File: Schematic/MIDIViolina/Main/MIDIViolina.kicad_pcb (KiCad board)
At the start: 2 copper layers, 149.9 x 101.6 mm, 152 parts, among them J1 Motor, J10 Solenoid, J11 Solenoid, J12 Solenoid, J13 Solenoid, J14 Solenoid, J15 Solenoid, J16 Solenoid, J17 Solenoid, J18 Solenoid, J19 Solenoid, J2 Motor, J20 Solenoid, J21 Solenoid, J22 Solenoid, J23 Solenoid, J24 Solenoid, J25 Solenoid, J26 Solenoid, J27 Solenoid, J28 Solenoid, J29 Solenoid, J3 Motor, J30 Solenoid, J31 Solenoid, J32 Solenoid, J33 Solenoid, J34 Solenoid, J35 Solenoid, J36 Solenoid, J37 Solenoid, J38 Solenoid, J39 Solenoid, J4 Motor, J40 Solenoid, J41 Solenoid, J5 Power in, J6 MSB 2, J7 Microstep Bridge, J8 MIDI I/O, J9 STEPPER OUT, Q1 IRF540N, Q10 IRF540N, Q11 IRF540N, Q12 IRF540N, Q13 IRF540N, Q14 IRF540N, Q15 IRF540N, Q16 IRF540N, Q17 IRF540N, Q18 IRF540N, Q19 IRF540N, Q2 IRF540N, Q20 IRF540N, Q21 IRF540N, Q22 IRF540N, Q23 IRF540N, Q24 IRF540N, Q25 IRF540N, Q26 IRF540N, Q27 IRF540N, Q28 IRF540N, Q29 IRF540N, Q3 IRF540N, Q30 IRF540N, Q31 IRF540N, Q32 IRF540N, Q33 IRF540N, Q34 IRF540N, Q35 IRF540N, Q36 IRF540N, Q4 IRF540N, Q5 IRF540N, Q6 IRF540N, Q7 IRF540N, Q8 IRF540N, Q9 IRF540N, U1 LM7805_TO220, U2 ESP32-DEVKIT-V1, U3 74AHC595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

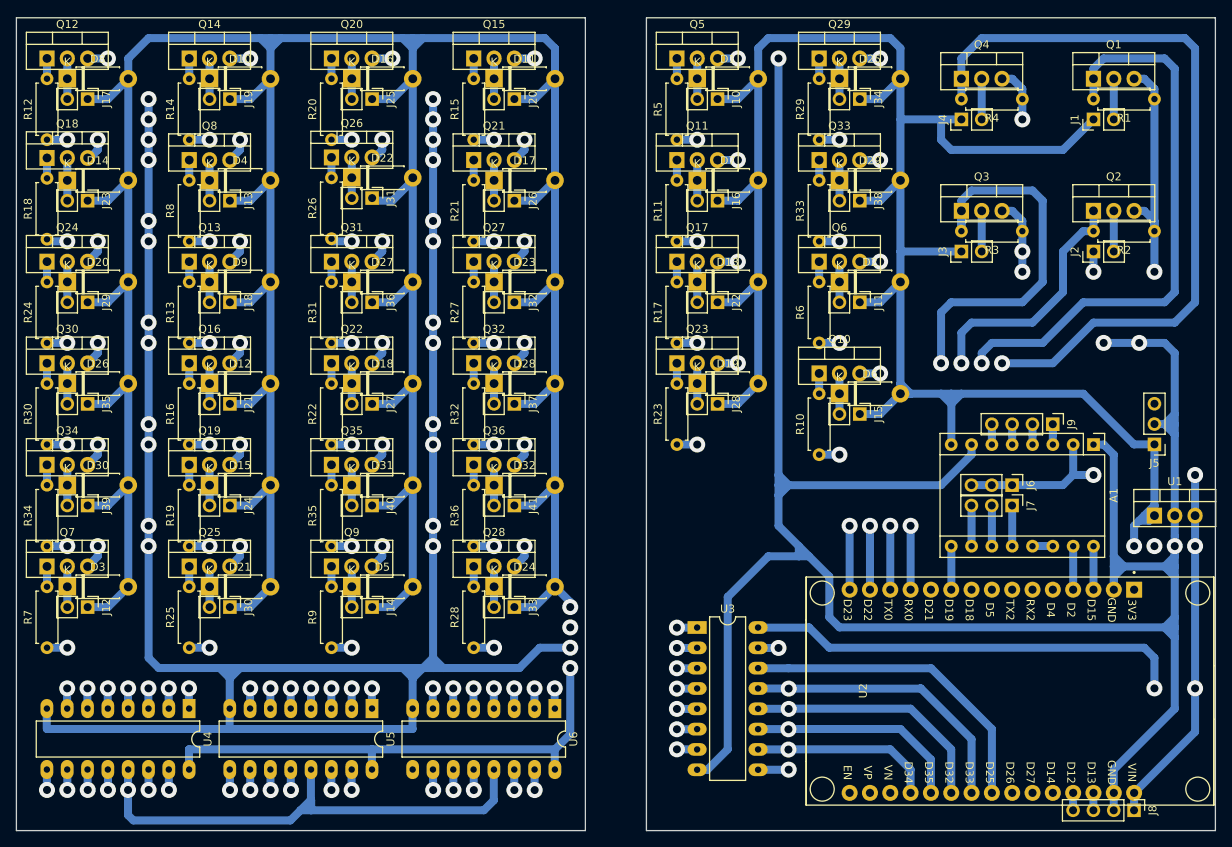
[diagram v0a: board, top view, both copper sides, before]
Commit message: CNC Toolpaths and PCB updates
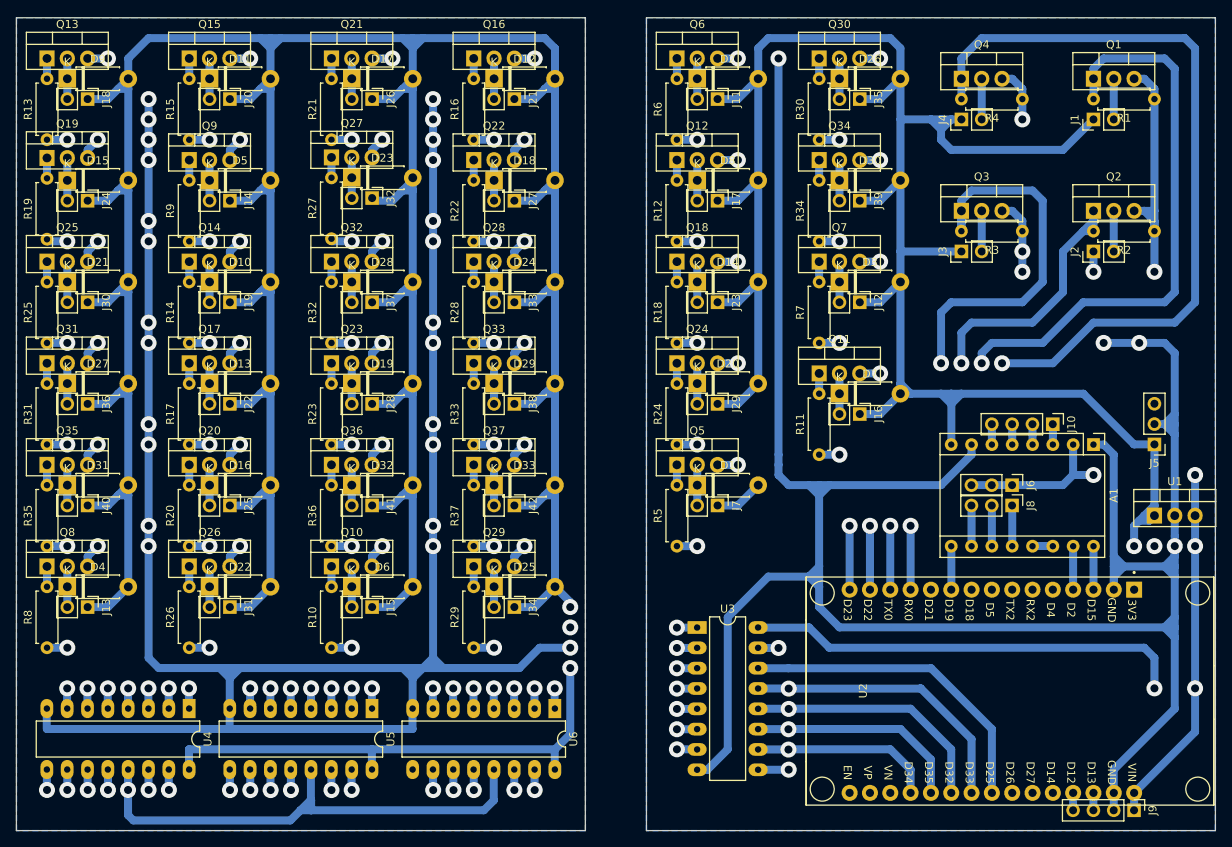
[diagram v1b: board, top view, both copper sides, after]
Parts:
- added D1: IN4001, Diode_THT:D_DO-41_SOD81_P7.62mm_Horizontal, F.Cu at (153.7, 96.5)
- added J7: Solenoid, Connector_PinHeader_2.54mm:PinHeader_1x02_P2.54mm_Vertical, F.Cu at (156.2, 99.1)
- added Q5: IRF540N, Package_TO_SOT_THT:TO-220-3_Vertical, F.Cu at (151.1, 94.0)
- added R5: 220, Resistor_THT:R_Axial_DIN0207_L6.3mm_D2.5mm_P7.62mm_Horizontal, F.Cu at (151.1, 104.1)
- renumbered D9 to D10, D10 to D11, D11 to D12, D12 to D13, D13 to D14, D14 to D15, D15 to D16, D16 to D17, D17 to D18, D18 to D19, D1 to D2, D19 to D20, D20 to D21, D21 to D22, D22 to D23, D23 to D24, D24 to D25, D25 to D26, D26 to D27, D27 to D28, D28 to D29, D2 to D3, D29 to D30, D30 to D31, D31 to D32, D32 to D33, D3 to D4, D4 to D5, D5 to D6, D6 to D7, D7 to D8, D8 to D9, J9 to J10, J10 to J11, J11 to J12, J12 to J13, J13 to J14, J14 to J15, J15 to J16, J16 to J17, J17 to J18, J18 to J19, J19 to J20, J20 to J21, J21 to J22, J22 to J23, J23 to J24, J24 to J25, J25 to J26, J26 to J27, J27 to J28, J28 to J29, J29 to J30, J30 to J31, J31 to J32, J32 to J33, J33 to J34, J34 to J35, J35 to J36, J36 to J37, J37 to J38, J38 to J39, J39 to J40, J40 to J41, J41 to J42, J7 to J8, J8 to J9, Q9 to Q10, Q10 to Q11, Q11 to Q12, Q12 to Q13, Q13 to Q14, Q14 to Q15, Q15 to Q16, Q16 to Q17, Q17 to Q18, Q18 to Q19, Q19 to Q20, Q20 to Q21, Q21 to Q22, Q22 to Q23, Q23 to Q24, Q24 to Q25, Q25 to Q26, Q26 to Q27, Q27 to Q28, Q28 to Q29, Q29 to Q30, Q30 to Q31, Q31 to Q32, Q32 to Q33, Q33 to Q34, Q34 to Q35, Q35 to Q36, Q36 to Q37, Q5 to Q6, Q6 to Q7, Q7 to Q8, Q8 to Q9, R9 to R10, R10 to R11, R11 to R12, R12 to R13, R13 to R14, R14 to R15, R15 to R16, R16 to R17, R17 to R18, R18 to R19, R19 to R20, R20 to R21, R21 to R22, R22 to R23, R23 to R24, R24 to R25, R25 to R26, R26 to R27, R27 to R28, R28 to R29, R29 to R30, R30 to R31, R31 to R32, R32 to R33, R33 to R34, R34 to R35, R35 to R36, R36 to R37, R5 to R6, R6 to R7, R7 to R8, R8 to R9
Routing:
- net +24V: track 742.2 -> 777.4 mm
- net Net-(D1-Pad1): track 0.00 -> 5.08 mm
- net Net-(Q5-Pad1): track 0.00 -> 2.54 mm
- net /Step: track 5.44 -> 7.98 mm, vias 0 -> 1
- net /Motor 3: track 39.1 -> 40.9 mm
- net GND: track 709.5 -> 711.0 mm, vias 67 -> 66
- net (no net): vias 0 -> 2
- added copper zone on B.Cu, net GND

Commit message: CAM and PCB manufacture
Generated CAM instructions for CNC mill
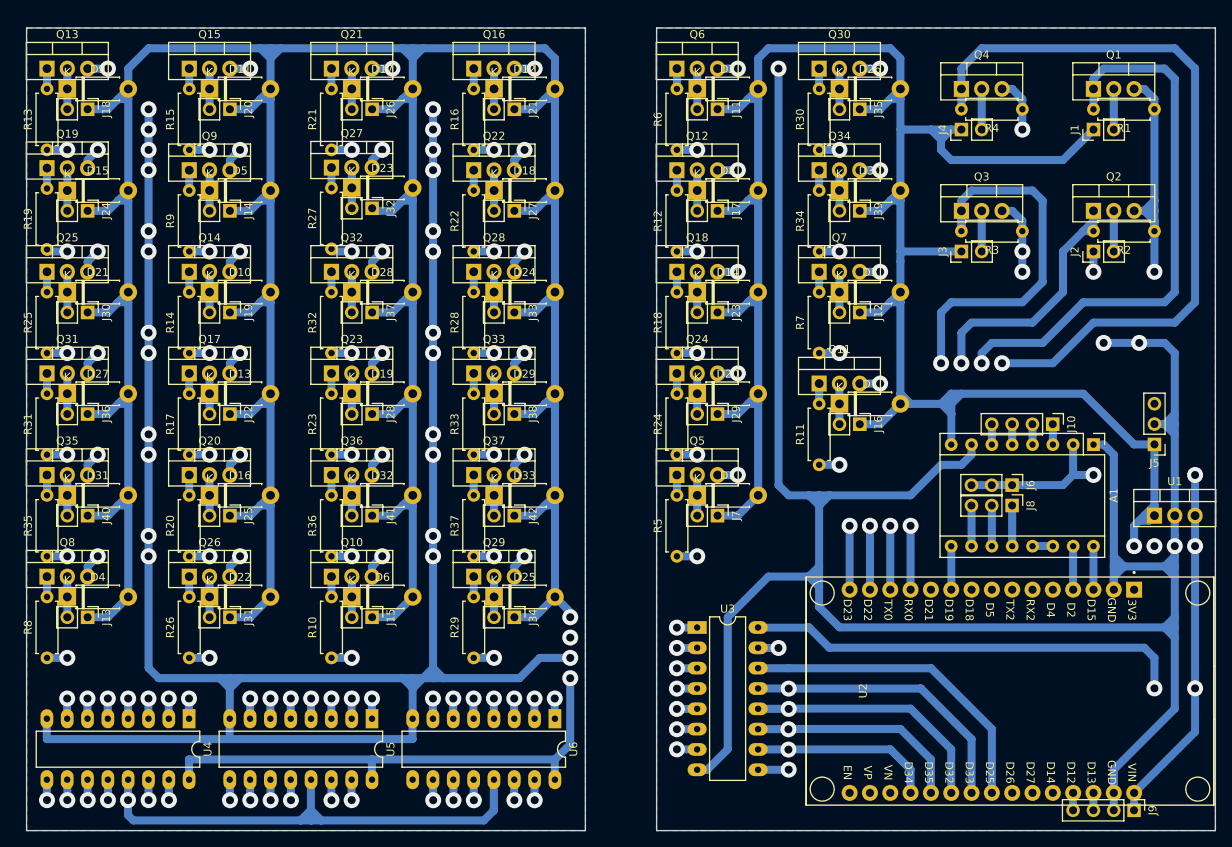
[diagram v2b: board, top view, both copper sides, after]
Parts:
- moved D1 1.27 mm to (153.7, 97.8)
- moved D13 1.27 mm to (92.7, 85.1)
- moved D16 1.27 mm to (92.7, 97.8)
- moved D19 1.27 mm to (110.5, 85.1)
- moved D20 1.27 mm to (153.7, 85.1)
- moved D27 1.27 mm to (74.9, 85.1)
- moved D29 1.27 mm to (128.3, 85.1)
- moved D31 1.27 mm to (74.9, 97.8)
- moved D32 1.27 mm to (110.5, 97.8)
- moved D33 1.27 mm to (128.3, 97.8)
- moved J12 1.27 mm to (174.0, 74.9)
- moved J16 1.27 mm to (174.0, 88.9)
- moved J19 1.27 mm to (95.2, 74.9)
- moved J23 1.27 mm to (156.2, 74.9)
- moved J30 1.27 mm to (77.5, 74.9)
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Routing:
- net +24V: track 777.4 -> 800.8 mm
- net /Motor 4: track 102.9 -> 100.9 mm
- net /Motor 1: track 79.5 -> 78.2 mm
- net GND: track 711.0 -> 712.0 mm
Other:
- board size 149.9 x 101.6 mm -> 148.6 x 100.3 mm
